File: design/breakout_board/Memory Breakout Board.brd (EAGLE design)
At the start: 90.2 x 60.2 mm, 1 part

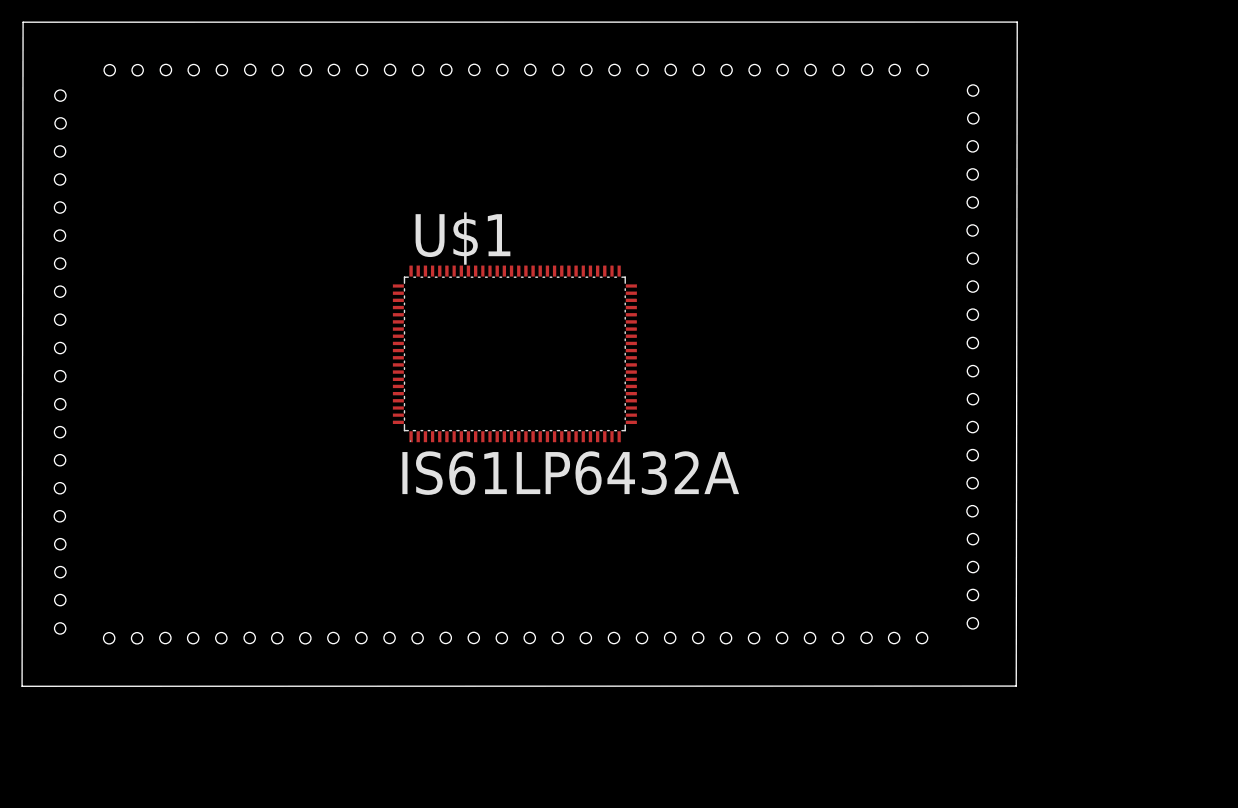
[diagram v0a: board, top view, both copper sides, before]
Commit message: board just needs silk screen layer
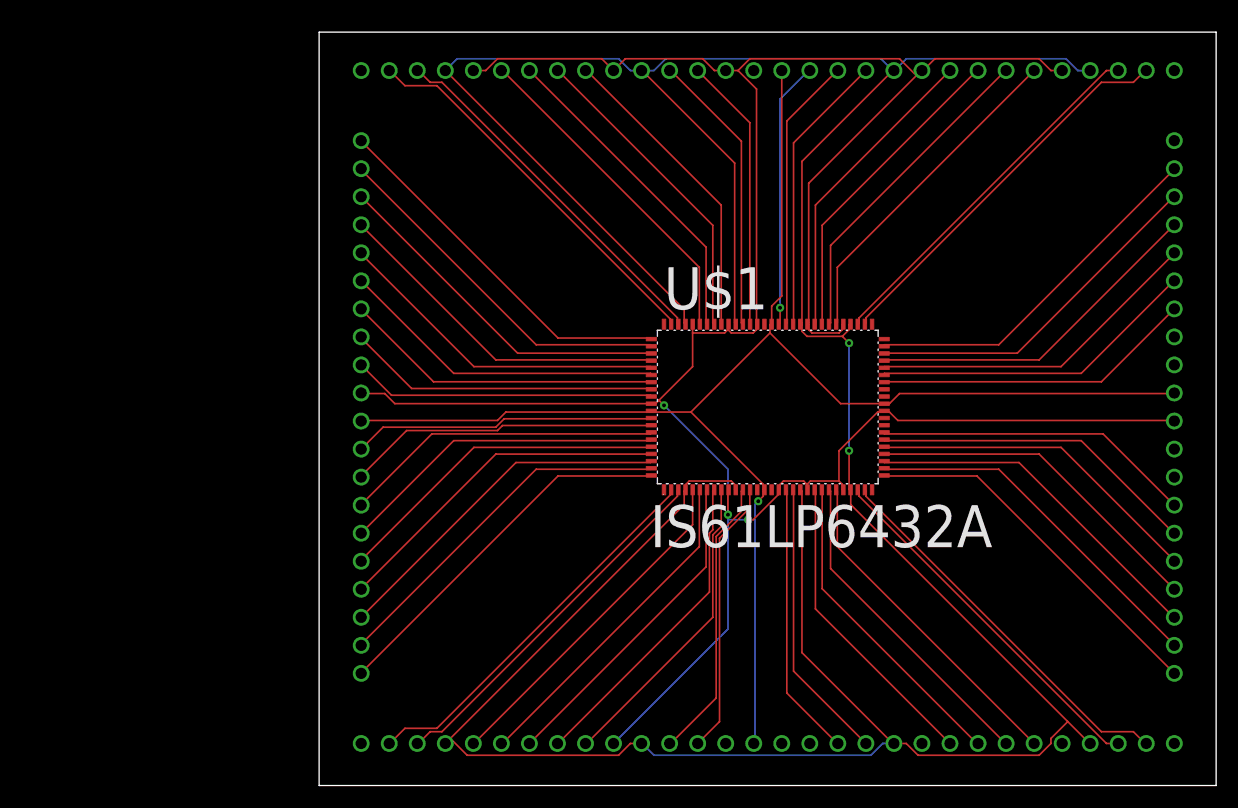
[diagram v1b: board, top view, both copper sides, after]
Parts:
- added U$2, U$3: HEADER20, memory:HEADER20
- added U$4, U$5: HEADER30, memory:HEADER30
- moved U$1 23.4 mm to (82.5, 49.5)
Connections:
- removed net +3V3: U$1.11, U$1.15, U$1.20, U$1.27, U$1.4, U$1.41, U$1.54, U$1.61, U$1.65, U$1.70, U$1.77, U$1.91
- removed net A0: U$1.37
- removed net A1: U$1.36
- removed net A10: U$1.44
- removed net A12: U$1.45
- removed net A13: U$1.47
- removed net A14: U$1.48
- removed net A15: U$1.49
- removed net A2: U$1.35
- removed net A3: U$1.34
- removed net A4: U$1.33
- removed net A5: U$1.32
- removed net CE2OVERLINE: U$1.92
- removed net DQA1: U$1.52
- removed net DQA2: U$1.53
- removed net DQA3: U$1.56
- removed net DQA4: U$1.57
- removed net DQA5: U$1.58
- removed net DQA6: U$1.59
- removed net DQA7: U$1.62
- removed net DQA8: U$1.63
- removed net DQB1: U$1.68
- removed net DQB2: U$1.69
- removed net DQB3: U$1.72
- removed net DQB4: U$1.73
- removed net DQB5: U$1.74
- removed net DQB6: U$1.75
- removed net DQB7: U$1.78
- removed net DQB8: U$1.79
- removed net DQC1: U$1.2
- removed net DQC2: U$1.3
- removed net DQC3: U$1.6
- removed net DQC4: U$1.7
- removed net DQC5: U$1.8
- removed net DQC6: U$1.9
- removed net DQC7: U$1.12
- removed net DQC8: U$1.13
- removed net DQD1: U$1.18
- removed net DQD2: U$1.19
- removed net DQD3: U$1.22
- removed net DQD4: U$1.23
- removed net DQD5: U$1.24
- removed net DQD6: U$1.25
- removed net DQD7: U$1.28
- removed net DQD8: U$1.29
- removed net DQPA: U$1.51
- removed net DQPB: U$1.80
- removed net DQPC: U$1.1
- removed net DQPD: U$1.30
- removed net GND: U$1.10, U$1.17, U$1.21, U$1.26, U$1.40, U$1.5, U$1.55, U$1.60, U$1.67, U$1.71, U$1.76, U$1.90
- removed net MODE: U$1.31
- removed net ZZ: U$1.64
- new net DBQ8: U$1.79, U$5.P$29
- new net N$1: U$1.2, U$4.P$2
- new net N$10: U$1.12, U$4.P$12
- new net N$11: U$1.13, U$4.P$13
- new net N$13: U$1.18, U$4.P$18
- new net N$15: U$1.22, U$4.P$22
- new net N$16: U$1.23, U$4.P$23
- new net N$17: U$1.24, U$4.P$24
- new net N$18: U$1.25, U$4.P$25
- new net N$19: U$1.28, U$4.P$28
- new net N$2: U$1.3, U$4.P$3
- new net N$20: U$1.29, U$4.P$29
- new net N$21: U$1.33, U$2.P$3
- new net N$22: U$1.11, U$1.20, U$1.27, U$1.4, U$1.54, U$1.61, U$1.70, U$1.77, U$4.P$11, U$4.P$20, U$4.P$27, U$4.P$4, U$5.P$11, U$5.P$20, U$5.P$27, U$5.P$4
- new net N$24: U$1.34, U$2.P$4
- new net N$25: U$1.35, U$2.P$5
- new net N$26: U$1.36, U$2.P$6
- new net N$27: U$1.37, U$2.P$7
- new net N$28: U$1.44, U$2.P$14
- new net N$29: U$1.45, U$2.P$15
- new net N$3: U$1.31, U$2.P$1
- new net N$30: U$1.46, U$2.P$16
- new net N$31: U$1.47, U$2.P$17
- new net N$32: U$1.48, U$2.P$18
- new net N$33: U$1.49, U$2.P$19
- new net N$34: U$1.52, U$5.P$2
- new net N$35: U$1.53, U$5.P$3
- new net N$36: U$1.56, U$5.P$6
- new net N$37: U$1.57, U$5.P$7
- new net N$38: U$1.58, U$5.P$8
- new net N$39: U$1.59, U$5.P$9
- new net N$4: U$1.5, U$4.P$5
- new net N$40: U$1.62, U$5.P$12
- new net N$41: U$1.63, U$5.P$13
- new net N$42: U$1.64, U$5.P$14
- new net N$43: U$1.68, U$5.P$18
- new net N$44: U$1.69, U$5.P$19
- new net N$45: U$1.72, U$5.P$22
- new net N$46: U$1.73, U$5.P$23
- new net N$47: U$1.74, U$5.P$24
- new net N$48: U$1.75, U$5.P$25
- new net N$49: U$1.78, U$5.P$28
- new net N$5: U$1.6, U$4.P$6
- new net N$6: U$1.7, U$4.P$7
- new net N$7: U$1.8, U$4.P$8
- new net N$8: U$1.9, U$4.P$9
- new net N$9: U$1.32, U$2.P$2
- new net VDD: U$1.15, U$1.41, U$1.65, U$1.91, U$2.P$11, U$3.P$11, U$4.P$15, U$5.P$15
- new net VSS: U$1.10, U$1.17, U$1.21, U$1.26, U$1.40, U$1.55, U$1.60, U$1.67, U$1.71, U$1.76, U$1.90, U$2.P$10, U$3.P$10, U$4.P$10, U$5.P$10, U$5.P$17, U$5.P$21, U$5.P$26, U$5.P$5
- new net _CE2: U$1.92, U$3.P$12
- net A6: now also U$3.P$20
- net A7: now also U$3.P$19
- net A8: now also U$3.P$2
- net A9: now also U$3.P$1
- net ADSC: now also U$3.P$5
- net ADSP: now also U$3.P$4
- net ADV: now also U$3.P$3
- net BW1: now also U$3.P$13
- net BW2: now also U$3.P$14
- net BW3: now also U$3.P$15
- net BW4: now also U$3.P$16
- net BWE: now also U$3.P$7
- net CE: now also U$3.P$18
- net CE2: now also U$3.P$17
- net CLK: now also U$3.P$9
- net GW: now also U$3.P$8
- net N$14: now also U$1.19, U$4.P$19; no longer U$1.46
- net OE: now also U$3.P$6
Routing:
- net N$22: track 0.00 -> 322.6 mm, vias 0 -> 2
- net VSS: track 0.00 -> 245.6 mm, vias 0 -> 3
- net VDD: track 0.00 -> 137.7 mm, vias 0 -> 1
- net N$34: track 0.00 -> 35.3 mm
- net N$20: track 0.00 -> 35.3 mm
- net DBQ8: track 0.00 -> 35.3 mm
- net N$1: track 0.00 -> 35.3 mm
- net A9: track 0.00 -> 33.8 mm
- net A6: track 0.00 -> 33.7 mm
- net N$3: track 0.00 -> 33.7 mm
- net N$49: track 0.00 -> 33.5 mm
- net N$2: track 0.00 -> 33.5 mm
- net N$35: track 0.00 -> 33.4 mm
- net N$19: track 0.00 -> 33.4 mm
- net A8: track 0.00 -> 33.0 mm
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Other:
- board size 90.2 x 60.2 mm -> 81.3 x 68.2 mm
